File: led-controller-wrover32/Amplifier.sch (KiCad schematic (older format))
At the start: 6 parts, among them J10 Conn_01x02 DNF, J11 Conn_01x02, U5 MAX98357A

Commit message: Minor changes
- Tweaked some of the component values in the 12V supply as per TI.
- Removed unnecessary protection diode, the USB one is enough.
- Changed UART to CS2104 which eliminates two resistors and is
  slightly cheaper
- Updated PCB to reflect changes.

Signed-off-by: Aaron Williams <aaron.w2@gmail.com>
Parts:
- C20: DESC (none) -> CAP CER 10UF 16V X7R 0805; MFR - -> Samsung; MPN - -> CL21B106KOQNNNE; SPN - -> 1276-2872-1-ND; SPR - -> Digikey
- C21, C22: DESC (none) -> CAP CER 0.1UF 50V X7R 0603
- J10: DESC (none) -> CONN HEADER SMD 2POS 1.27MM
- J11: DESC (none) -> CONN HEADER SMD 2POS 1MM
- U5: DESC (none) -> IC AMP CLASS D MONO 3.2W 16TQFN
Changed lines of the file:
@@
 F 7 "MAX98357AETE+TCT-ND" H 3900 3200 50  0001 C CNN "SPN"
 F 8 "https://www.digikey.com/products/en/integrated-circuits-ics/linear-amplifiers-audio/742?k=MAX98357A&k=&pkeyword=MAX98357A&sv=0&pv7=2&pv1291=108687&pv16=108891&sf=0&FV=-8%7C742&quantity=&ColumnSort=0&page=1&pageSize=500" H 3900 3200 50  0001 C CNN "SPURL"
+F 9 "IC AMP CLASS D MONO 3.2W 16TQFN" H 0   0   50  0001 C CNN "DESC"
 	1    3900 3200
 	1    0    0    -1
@@
 F 1 "10uF" H 4565 2605 50  0000 L CNN
 F 2 "Capacitor_SMD:C_0805_2012Metric" H 4488 2500 50  0001 C CNN
-F 3 "~" H 4450 2650 50  0001 C CNN
-F 4 "-" H 0   0   50  0001 C CNN "MFR"
-F 5 "-" H 0   0   50  0001 C CNN "MPN"
-F 6 "-" H 0   0   50  0001 C CNN "SPR"
-F 7 "-" H 0   0   50  0001 C CNN "SPN"
+F 3 "http://www.samsungsem.com/kr/support/product-search/mlcc/CL21B106KOQNNNE.jsp" H 4450 2650 50  0001 C CNN
+F 4 "Samsung" H 0   0   50  0001 C CNN "MFR"
+F 5 "CL21B106KOQNNNE" H 0   0   50  0001 C CNN "MPN"
+F 6 "Digikey" H 0   0   50  0001 C CNN "SPR"
+F 7 "1276-2872-1-ND" H 0   0   50  0001 C CNN "SPN"
 F 8 "-" H 0   0   50  0001 C CNN "SPURL"
+F 9 "CAP CER 10UF 16V X7R 0805" H 0   0   50  0001 C CNN "DESC"
 	1    4450 2650
 	1    0    0    -1
@@
 F 7 "490-4779-1-ND" H 0   0   50  0001 C CNN "SPN"
 F 8 "-" H 0   0   50  0001 C CNN "SPURL"
+F 9 "CAP CER 0.1UF 50V X7R 0603" H 0   0   50  0001 C CNN "DESC"
 	1    4850 2650
 	1    0    0    -1
@@
 F 7 "490-4779-1-ND" H 0   0   50  0001 C CNN "SPN"
 F 8 "-" H 0   0   50  0001 C CNN "SPURL"
+F 9 "CAP CER 0.1UF 50V X7R 0603" H 0   0   50  0001 C CNN "DESC"
 	1    3000 2800
 	1    0    0    -1
@@
 F 7 "455-1788-1-ND" H 5200 3200 50  0001 C CNN "SPN"
 F 8 "https://www.digikey.com/product-detail/en/jst-sales-america-inc/BM02B-SRSS-TB-LF-SN/455-1788-1-ND/926859" H 5200 3200 50  0001 C CNN "SPURL"
+F 9 "CONN HEADER SMD 2POS 1MM" H 0   0   50  0001 C CNN "DESC"
 	1    5200 3200
 	1    0    0    -1
@@
 F 7 "952-3933-1-ND" H 5200 3600 50  0001 C CNN "SPN"
 F 8 "https://www.digikey.com/products/en/connectors-interconnects/rectangular-connectors-headers-male-pins/314?k=M50-3630242R&k=&pkeyword=M50-3630242R&sv=0&pv7=2&sf=0&quantity=&ColumnSort=0&page=1&stock=1&nstock=1&pageSize=500" H 5200 3600 50  0001 C CNN "SPURL"
+F 9 "CONN HEADER SMD 2POS 1.27MM" H 0   0   50  0001 C CNN "DESC"
 	1    5200 3600
 	1    0    0    -1

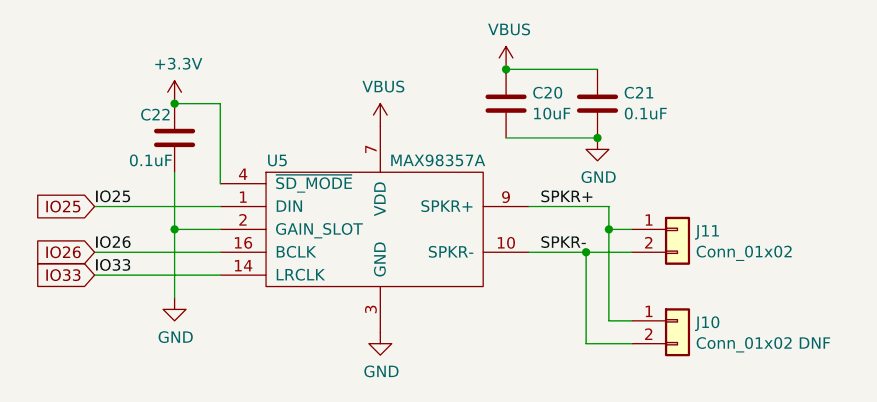
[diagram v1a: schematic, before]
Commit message: Multiple changes from v3.7
1. Fixed microphone so it uses the left channel
2. Reduced the number of unique components, i.e. replacing a couple of
   resistor networks with already used resistors
3. Removed unneeded resistor in programming circuit
4. Moved speaker chip to the other side to be closer to the connector
5. Cleaned up some of the traces and removed some inner-layer traces.
6. Moved reset switch to the edge to make access easier.
7. Added big via to line up with daughter card.
8. Replaced BSS138 transistor array with two BSS138 transistors to reduce
   the unique component count and reduce cost.

Signed-off-by: Aaron Williams <aaron.w2@gmail.com>
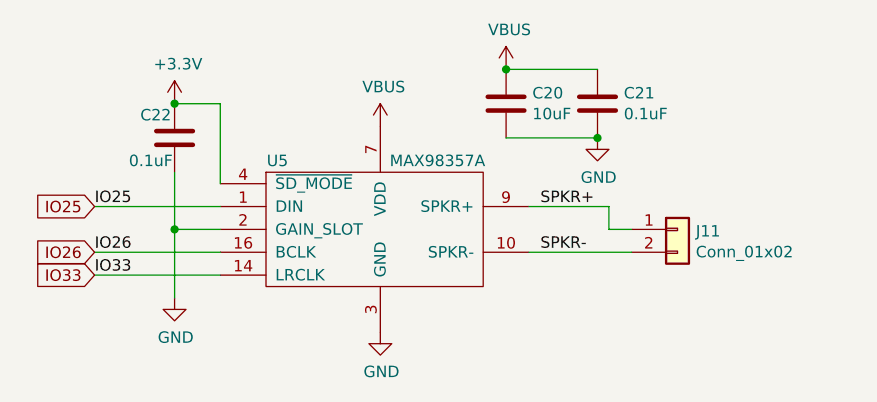
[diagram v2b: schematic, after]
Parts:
- removed J10: Conn_01x02 DNF, Connector_PinHeader_1.27mm:PinHeader_1x02_P1.27mm_Vertical_SMD_Pin1Left, symbol Connector_Generic:Conn_01x02
- C20: SPURL - -> https://www.digikey.com/products/en?keywords=1276-2872-1-ND
- C21, C22: SPURL - -> https://www.digikey.com/product-detail/en/murata-electronic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
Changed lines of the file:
@@
 F 6 "Digikey" H 0   0   50  0001 C CNN "SPR"
 F 7 "1276-2872-1-ND" H 0   0   50  0001 C CNN "SPN"
-F 8 "-" H 0   0   50  0001 C CNN "SPURL"
+F 8 "https://www.digikey.com/products/en?keywords=1276-2872-1-ND" H 0   0   50  0001 C CNN "SPURL"
 F 9 "CAP CER 10UF 16V X7R 0805" H 0   0   50  0001 C CNN "DESC"
 	1    4450 2650
@@
 F 6 "Digikey" H 0   0   50  0001 C CNN "SPR"
 F 7 "490-4779-1-ND" H 0   0   50  0001 C CNN "SPN"
-F 8 "-" H 0   0   50  0001 C CNN "SPURL"
+F 8 "https://www.digikey.com/product-detail/en/murata-electronics/GCM188R71H104KA57D/490-4779-1-ND/1641698" H 0   0   50  0001 C CNN "SPURL"
 F 9 "CAP CER 0.1UF 50V X7R 0603" H 0   0   50  0001 C CNN "DESC"
 	1    4850 2650
@@
 F 6 "Digikey" H 0   0   50  0001 C CNN "SPR"
 F 7 "490-4779-1-ND" H 0   0   50  0001 C CNN "SPN"
-F 8 "-" H 0   0   50  0001 C CNN "SPURL"
+F 8 "https://www.digikey.com/product-detail/en/murata-electronics/GCM188R71H104KA57D/490-4779-1-ND/1641698" H 0   0   50  0001 C CNN "SPURL"
 F 9 "CAP CER 0.1UF 50V X7R 0603" H 0   0   50  0001 C CNN "DESC"
 	1    3000 2800
@@
 F 9 "CONN HEADER SMD 2POS 1MM" H 0   0   50  0001 C CNN "DESC"
 	1    5200 3200
-	1    0    0    -1
-$EndComp
-$Comp
-L Connector_Generic:Conn_01x02 J10
-U 1 1 5E133F76
-P 5200 3600
-F 0 "J10" H 5280 3592 50  0000 L CNN
-F 1 "Conn_01x02 DNF" H 5280 3501 50  0000 L CNN
-F 2 "Connector_PinHeader_1.27mm:PinHeader_1x02_P1.27mm_Vertical_SMD_Pin1Left" H 5200 3600 50  0001 C CNN
-F 3 "https://media.digikey.com/pdf/Data%20Sheets/JST%20PDFs/SR%20Connector.pdf" H 5200 3600 50  0001 C CNN
-F 4 "Harwin Inc." H 5200 3600 50  0001 C CNN "MFR"
-F 5 "M50-3630242R" H 5200 3600 50  0001 C CNN "MPN"
-F 6 "Digikey" H 5200 3600 50  0001 C CNN "SPR"
-F 7 "952-3933-1-ND" H 5200 3600 50  0001 C CNN "SPN"
-F 8 "https://www.digikey.com/products/en/connectors-interconnects/rectangular-connectors-headers-male-pins/314?k=M50-3630242R&k=&pkeyword=M50-3630242R&sv=0&pv7=2&sf=0&quantity=&ColumnSort=0&page=1&stock=1&nstock=1&pageSize=500" H 5200 3600 50  0001 C CNN "SPURL"
-F 9 "CONN HEADER SMD 2POS 1.27MM" H 0   0   50  0001 C CNN "DESC"
-	1    5200 3600
 	1    0    0    -1
 $EndComp
@@
 	4900 3200 5000 3200
 Wire Wire Line
-	4550 3300 4800 3300
-Wire Wire Line
-	4900 3200 4900 3600
-Wire Wire Line
-	4900 3600 5000 3600
-Wire Wire Line
-	4800 3300 4800 3700
-Wire Wire Line
-	4800 3700 5000 3700
-Wire Wire Line
-	4800 3300 5000 3300
+	4550 3300 5000 3300
 Connection ~ 4850 2800
 Connection ~ 4450 2500
 Connection ~ 3000 2650
 Connection ~ 3000 3200
-Connection ~ 4900 3200
-Connection ~ 4800 3300
 $EndSCHEMATC
